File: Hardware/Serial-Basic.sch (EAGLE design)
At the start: 25 parts, among them J1 microB, U1 AP2112-3.3V, U2 CH340G, Y2 12MHz

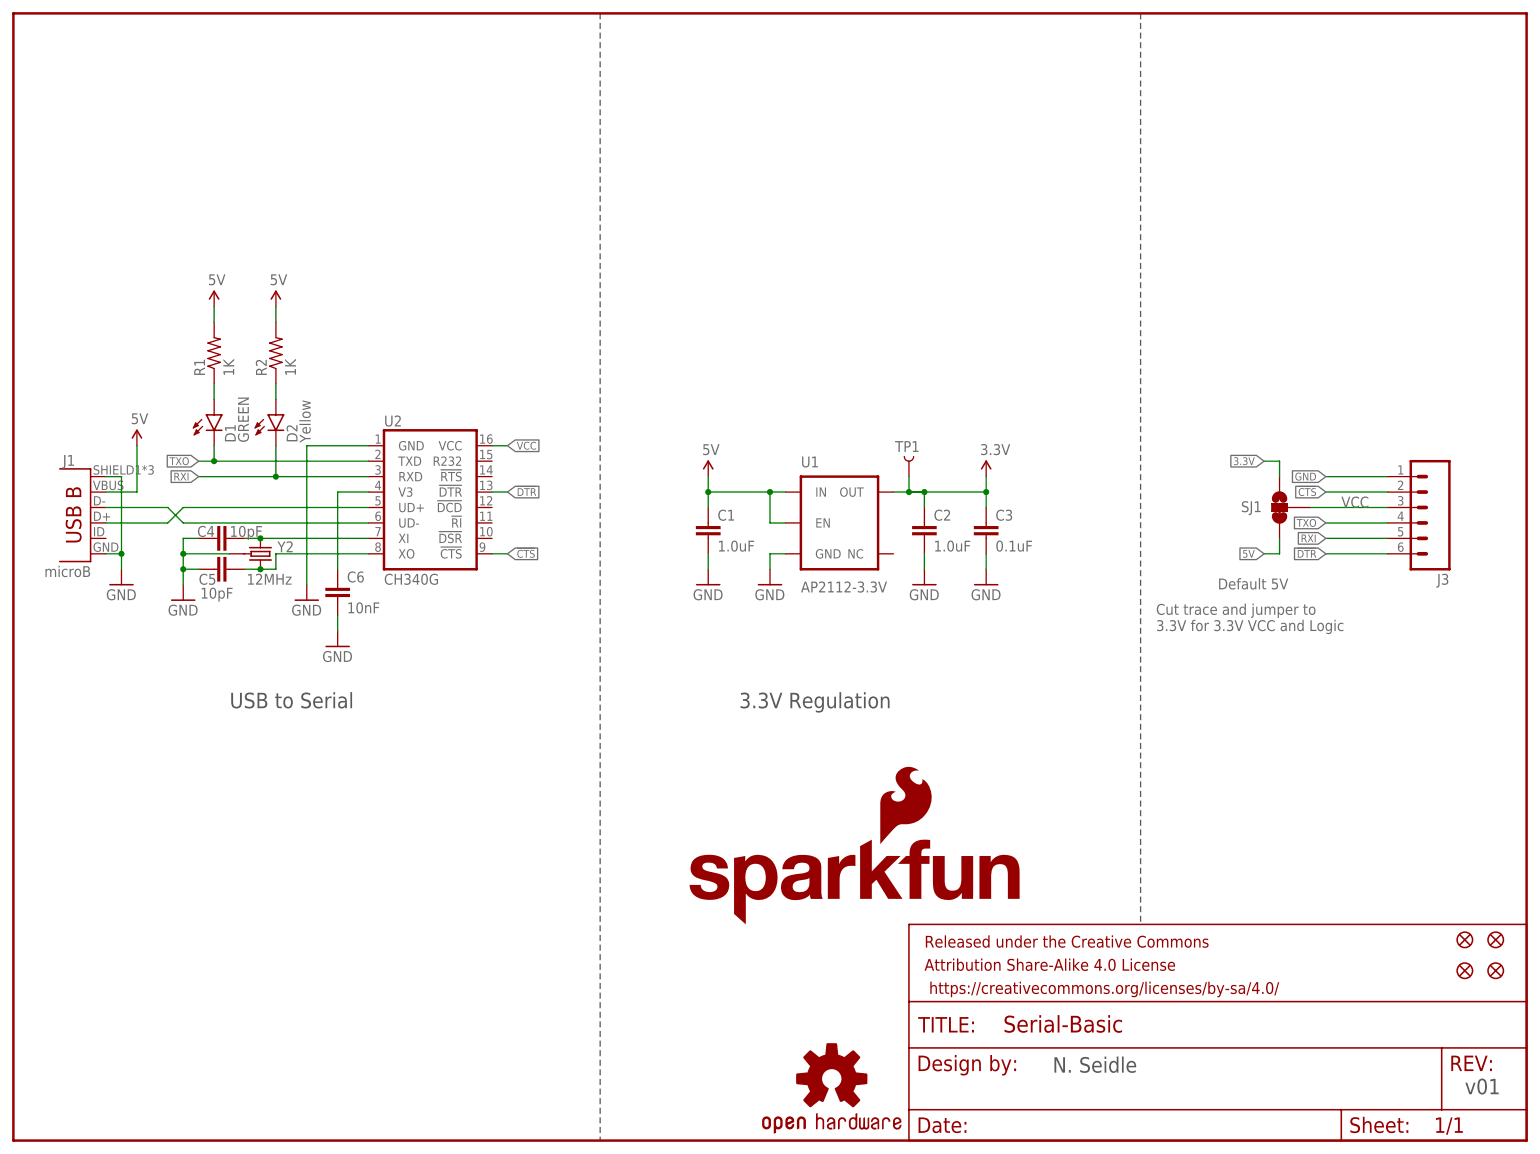
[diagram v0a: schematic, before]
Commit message: Many hardware changes from review.
Moved 0.1uF closer to IC, changed to VCC net. Added via anchors to
microB. Silk bumps. PCB width increase.
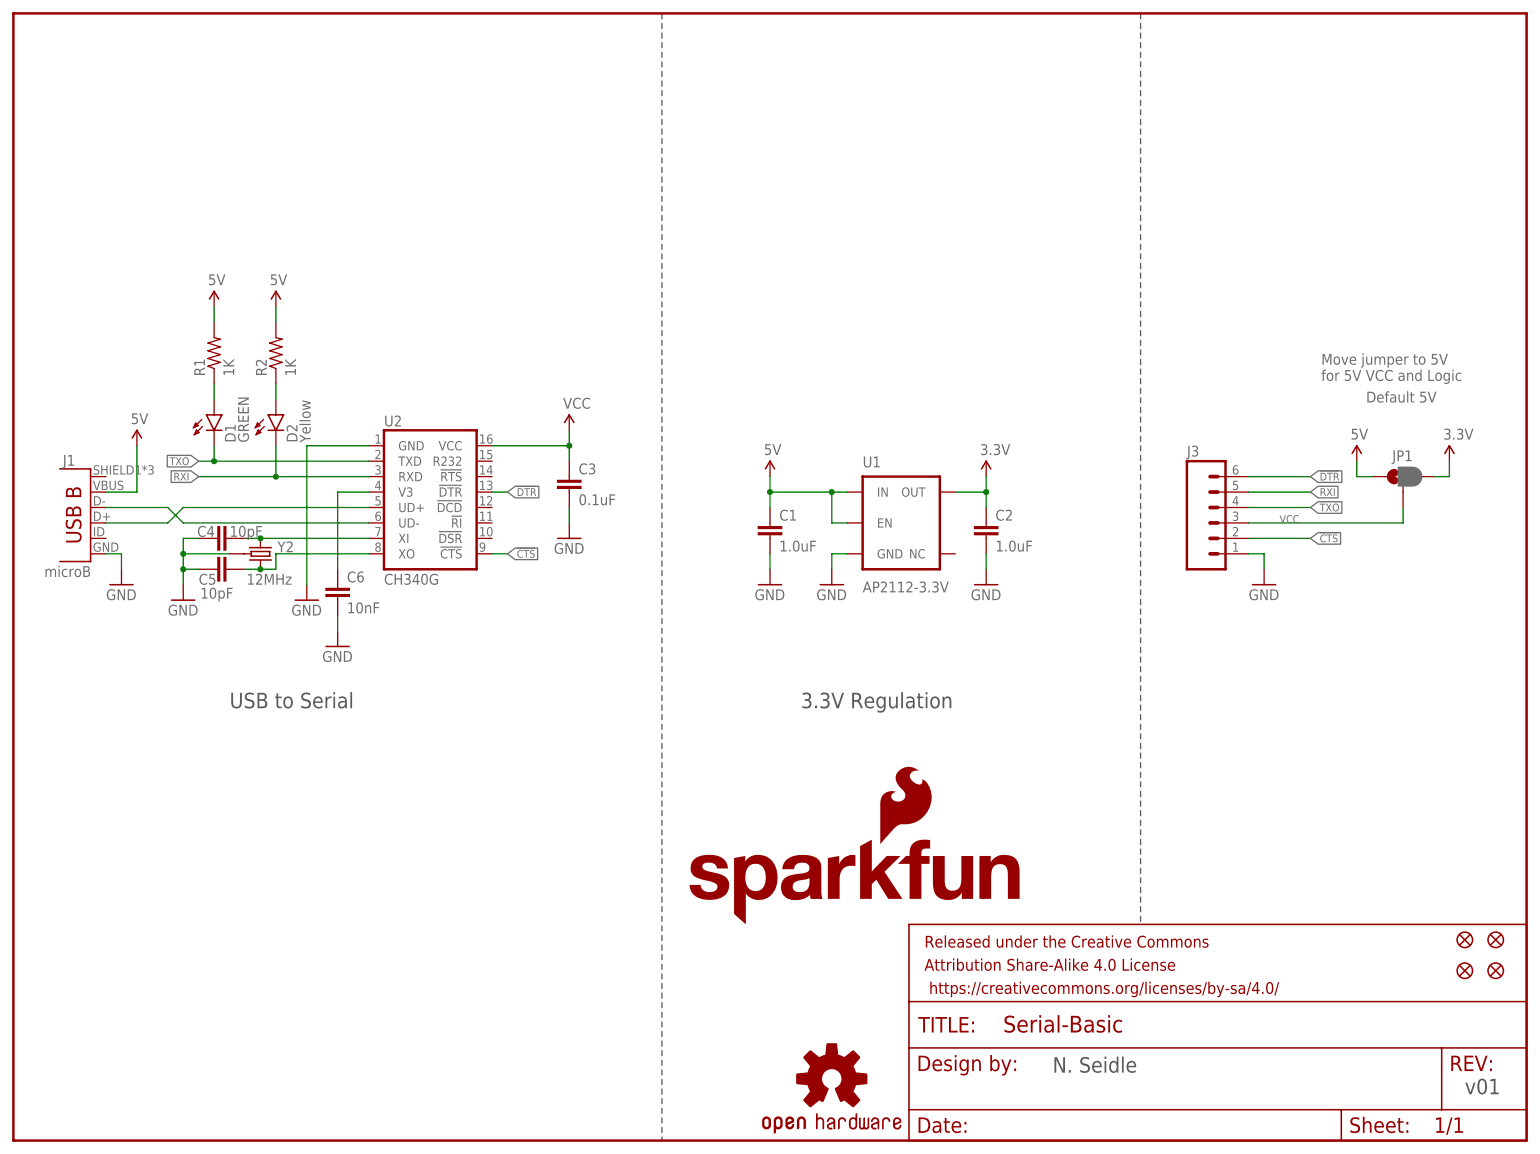
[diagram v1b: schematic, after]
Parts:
- removed SJ1: (no value), SparkFun:SOLDERJUMPER_2WAYS
- removed TP1: 3.3V TP, SparkFun-Passives:TEST-POINT3
- added JP1: JUMPER-PAD-3-2OF3_NC_BY_PASTE, SparkFun-Passives:JUMPER-PAD-3-2OF3_NC_BY_PASTE
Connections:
- net 3.3V: now also JP1.3; no longer C3.1, SJ1.3, TP1.1
- net 5V: now also JP1.1; no longer SJ1.1
- net GND: no longer J1.SHIELD
- net VCC: now also C3.1, JP1.2; no longer SJ1.2
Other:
- note added: "Move jumper to 5V for 5V VCC and Logic"
- note removed: "Cut trace and jumper to 3.3V for 3.3V VCC and Logic"
- moved on the sheet: C1, C2, C3, J3, U1

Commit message: Fixing issues #1, #2, #3, #4
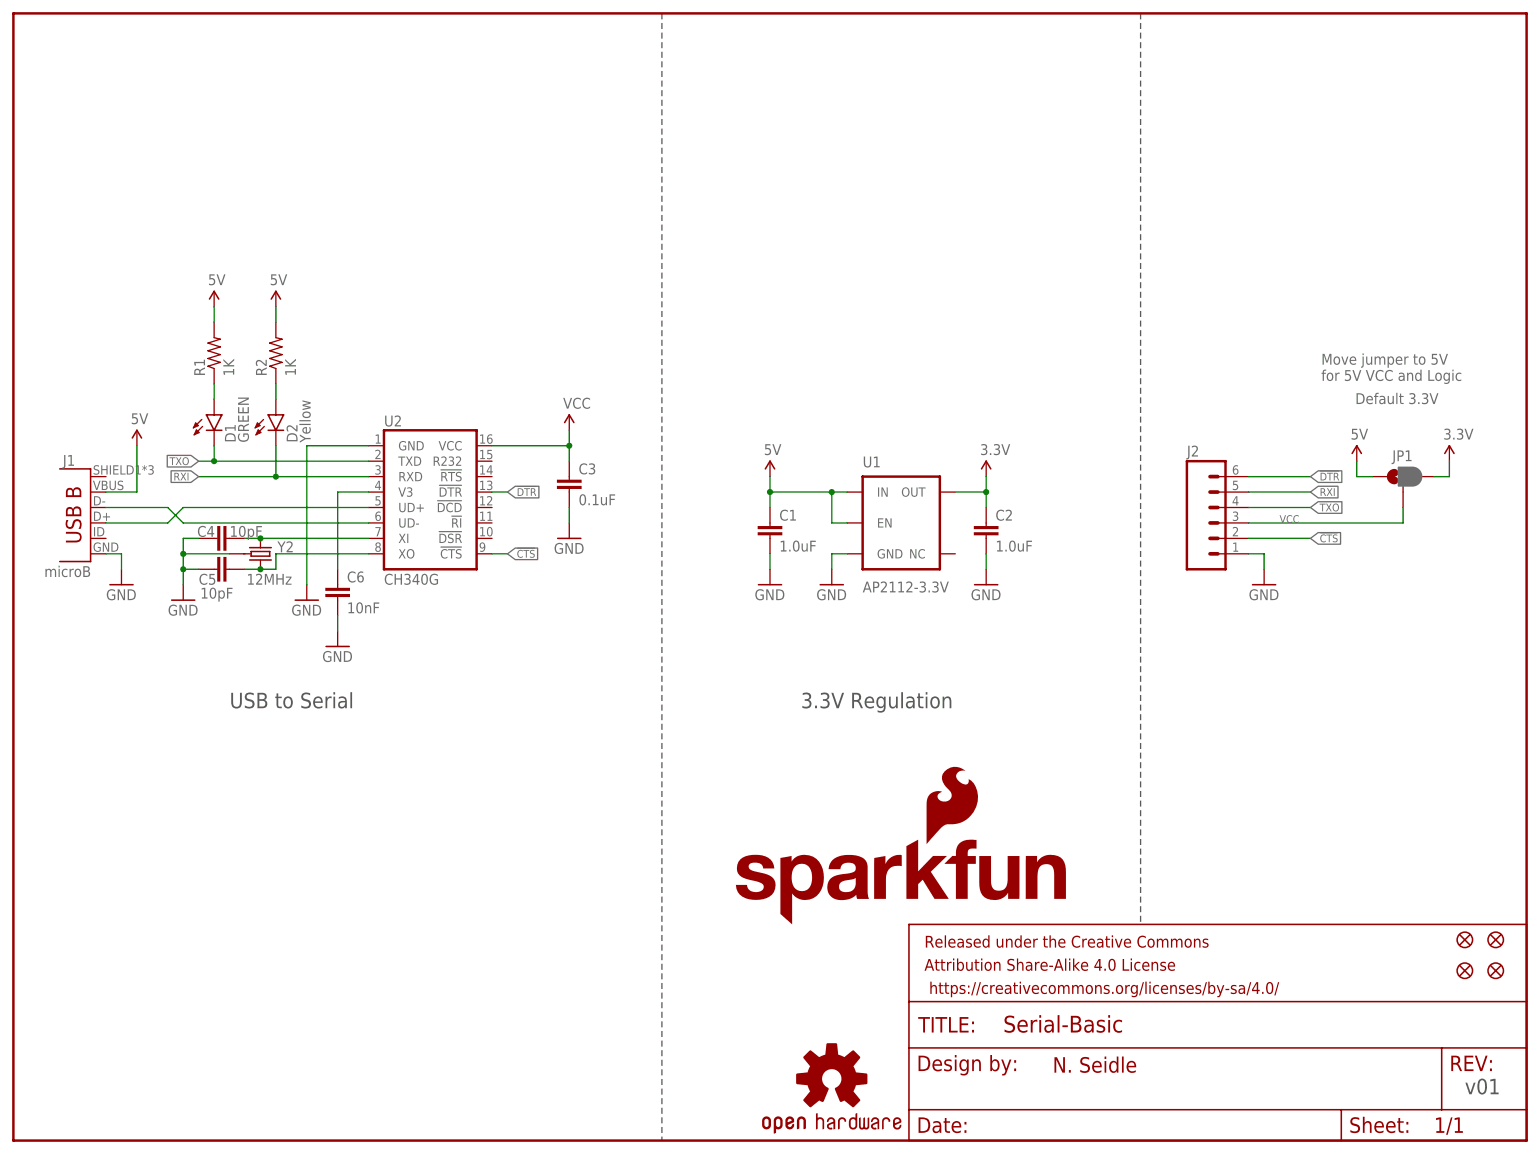
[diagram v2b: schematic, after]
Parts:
- renumbered J3 to J2
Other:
- note added: "Default 3.3V"
- note removed: "Default 5V"
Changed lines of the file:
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@@
 <?xml version="1.0" encoding="utf-8"?>
 <!DOCTYPE eagle SYSTEM "eagle.dtd">
-<eagle version="7.1.0">
+<eagle version="7.2.0">
 <drawing>
 <settings>
@@
 <part name="R2" library="SparkFun-Resistors" deviceset="1KOHM-1/10W-1%(0603)" device="" value="1K"/>
 <part name="C3" library="SparkFun-Capacitors" deviceset="0.1UF-25V(+80/-20%)(0603)" device="" value="0.1uF"/>
-<part name="J3" library="SparkFun-Connectors" deviceset="M06" device="SMD-FEMALE-V2"/>
+<part name="J2" library="SparkFun-Connectors" deviceset="M06" device="SMD-FEMALE-V2"/>
 <part name="SUPPLY2" library="SparkFun-Aesthetics" deviceset="VCC" device=""/>
 <part name="U$2" library="SparkFun" deviceset="5V" device=""/>
@@
 <sheet>
 <plain>
-<text x="222.504" y="121.412" size="1.778" layer="95">Default 5V</text>
+<text x="220.726" y="121.158" size="1.778" layer="95">Default 3.3V</text>
 <text x="238.76" y="7.62" size="2.54" layer="97">v01</text>
 <text x="35.56" y="71.12" size="2.54" layer="97">USB to Serial</text>
@@
 <wire x1="106.68" y1="185.42" x2="106.68" y2="0" width="0.2032" layer="97" style="longdash"/>
 <wire x1="185.42" y1="185.42" x2="185.42" y2="35.56" width="0.2032" layer="97" style="longdash"/>
-<text x="170.942" y="11.176" size="2.54" layer="97">N. Seidle</text>
+<text x="170.942" y="11.176" size="2.54" layer="94">N. Seidle</text>
 <text x="215.138" y="124.968" size="1.778" layer="95">Move jumper to 5V
 for 5V VCC and Logic</text>
@@
 <instance part="GND8" gate="1" x="53.34" y="81.28"/>
 <instance part="SUPPLY1" gate="G$1" x="160.02" y="109.22"/>
-<instance part="LOGO3" gate="G$1" x="109.22" y="35.56"/>
-<instance part="LOGO2" gate="G$1" x="142.24" y="48.26"/>
+<instance part="LOGO3" gate="G$1" x="116.84" y="35.56"/>
+<instance part="LOGO2" gate="G$1" x="149.86" y="48.26"/>
 <instance part="D1" gate="G$1" x="33.02" y="119.38"/>
 <instance part="D2" gate="G$1" x="43.18" y="119.38"/>
@@
 <instance part="R2" gate="G$1" x="43.18" y="129.54" rot="R90"/>
 <instance part="C3" gate="G$1" x="91.44" y="106.68"/>
-<instance part="J3" gate="G$1" x="198.12" y="101.6"/>
+<instance part="J2" gate="G$1" x="198.12" y="101.6"/>
 <instance part="SUPPLY2" gate="G$1" x="91.44" y="116.84"/>
 <instance part="U$2" gate="G$1" x="220.98" y="111.76"/>
@@
 <segment>
 <wire x1="203.2" y1="96.52" x2="205.74" y2="96.52" width="0.1524" layer="91"/>
-<pinref part="J3" gate="G$1" pin="1"/>
+<pinref part="J2" gate="G$1" pin="1"/>
 <pinref part="GND1" gate="1" pin="GND"/>
 <wire x1="205.74" y1="93.98" x2="205.74" y2="96.52" width="0.1524" layer="91"/>
@@
 <wire x1="203.2" y1="99.06" x2="213.36" y2="99.06" width="0.1524" layer="91"/>
 <label x="213.36" y="99.06" size="1.27" layer="95" xref="yes"/>
-<pinref part="J3" gate="G$1" pin="2"/>
+<pinref part="J2" gate="G$1" pin="2"/>
 </segment>
 <segment>
@@
 <wire x1="203.2" y1="109.22" x2="213.36" y2="109.22" width="0.1524" layer="91"/>
 <label x="213.36" y="109.22" size="1.27" layer="95" xref="yes"/>
-<pinref part="J3" gate="G$1" pin="6"/>
+<pinref part="J2" gate="G$1" pin="6"/>
 </segment>
 <segment>
@@
 <wire x1="203.2" y1="104.14" x2="213.36" y2="104.14" width="0.1524" layer="91"/>
 <label x="213.36" y="104.14" size="1.27" layer="95" xref="yes"/>
-<pinref part="J3" gate="G$1" pin="4"/>
+<pinref part="J2" gate="G$1" pin="4"/>
 </segment>
 <segment>
@@
 <wire x1="203.2" y1="106.68" x2="213.36" y2="106.68" width="0.1524" layer="91"/>
 <label x="213.36" y="106.68" size="1.27" layer="95" xref="yes"/>
-<pinref part="J3" gate="G$1" pin="5"/>
+<pinref part="J2" gate="G$1" pin="5"/>
 </segment>
 <segment>
@@
 <segment>
 <label x="208.28" y="101.6" size="1.27" layer="95"/>
-<pinref part="J3" gate="G$1" pin="3"/>
+<pinref part="J2" gate="G$1" pin="3"/>
 <wire x1="203.2" y1="101.6" x2="228.6" y2="101.6" width="0.1524" layer="91"/>
 <wire x1="228.6" y1="101.6" x2="228.6" y2="104.14" width="0.1524" layer="91"/>

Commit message: Changing resistor on Greeg LED to 330
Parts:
- removed R1: 1K, SparkFun-Resistors:1KOHM-1/10W-1%(0603)
- added R3: 330, SparkFun-Resistors:330OHM1/10W1%(0603)
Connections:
- net 5V: no longer R1.2, R2.2
- net N$1: now also R3.1; no longer R1.1
- net VCC: now also R2.2, R3.2
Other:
- note added: "v10"
- note removed: "v01"
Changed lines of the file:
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@@
 <part name="FRAME1" library="SparkFun-Aesthetics" deviceset="FRAME-LETTER" device=""/>
 <part name="GND7" library="SparkFun" deviceset="GND" device=""/>
-<part name="U$1" library="SparkFun" deviceset="5V" device=""/>
-<part name="U$4" library="SparkFun" deviceset="5V" device=""/>
 <part name="JP3" library="SparkFun" deviceset="FIDUCIAL" device="1X2"/>
 <part name="JP4" library="SparkFun" deviceset="FIDUCIAL" device="1X2"/>
@@
 <part name="D1" library="SparkFun-LED" deviceset="LED-GREEN" device="0603" value="GREEN"/>
 <part name="D2" library="SparkFun-LED" deviceset="LED-YELLOW" device="0603" value="Yellow"/>
-<part name="R1" library="SparkFun-Resistors" deviceset="1KOHM-1/10W-1%(0603)" device="" value="1K"/>
 <part name="R2" library="SparkFun-Resistors" deviceset="1KOHM-1/10W-1%(0603)" device="" value="1K"/>
 <part name="C3" library="SparkFun-Capacitors" deviceset="0.1UF-25V(+80/-20%)(0603)" device="" value="0.1uF"/>
@@
 <part name="GND1" library="SparkFun" deviceset="GND" device=""/>
 <part name="JP1" library="SparkFun-Passives" deviceset="JUMPER-PAD-3-2OF3_NC_BY_PASTE" device="" value=""/>
+<part name="SUPPLY4" library="SparkFun-Aesthetics" deviceset="VCC" device=""/>
+<part name="SUPPLY5" library="SparkFun-Aesthetics" deviceset="VCC" device=""/>
+<part name="R3" library="SparkFun-Resistors" deviceset="330OHM1/10W1%(0603)" device="" value="330"/>
 </parts>
 <sheets>
@@
 <plain>
 <text x="220.726" y="121.158" size="1.778" layer="95">Default 3.3V</text>
-<text x="238.76" y="7.62" size="2.54" layer="97">v01</text>
+<text x="238.76" y="7.62" size="2.54" layer="97">v10</text>
 <text x="35.56" y="71.12" size="2.54" layer="97">USB to Serial</text>
 <text x="129.54" y="71.12" size="2.54" layer="97">3.3V Regulation</text>
@@
 <instance part="FRAME1" gate="V" x="147.32" y="0"/>
 <instance part="GND7" gate="1" x="91.44" y="99.06"/>
-<instance part="U$1" gate="G$1" x="33.02" y="137.16"/>
-<instance part="U$4" gate="G$1" x="43.18" y="137.16"/>
 <instance part="JP3" gate="G$1" x="238.76" y="27.94"/>
 <instance part="JP4" gate="G$1" x="243.84" y="27.94"/>
@@
 <instance part="D1" gate="G$1" x="33.02" y="119.38"/>
 <instance part="D2" gate="G$1" x="43.18" y="119.38"/>
-<instance part="R1" gate="G$1" x="33.02" y="129.54" rot="R90"/>
 <instance part="R2" gate="G$1" x="43.18" y="129.54" rot="R90"/>
 <instance part="C3" gate="G$1" x="91.44" y="106.68"/>
@@
 <attribute name="VALUE" x="230.505" y="111.76" size="1.778" layer="96" rot="R90"/>
 </instance>
+<instance part="SUPPLY4" gate="G$1" x="43.18" y="137.16"/>
+<instance part="SUPPLY5" gate="G$1" x="33.02" y="137.16"/>
+<instance part="R3" gate="G$1" x="33.02" y="129.54" rot="R90"/>
 </instances>
 <busses>
@@
 <wire x1="33.02" y1="124.46" x2="33.02" y2="121.92" width="0.1524" layer="91"/>
 <pinref part="D1" gate="G$1" pin="A"/>
-<pinref part="R1" gate="G$1" pin="1"/>
+<pinref part="R3" gate="G$1" pin="1"/>
 </segment>
 </net>
@@
 <wire x1="91.44" y1="116.84" x2="91.44" y2="114.3" width="0.1524" layer="91"/>
 </segment>
+<segment>
+<wire x1="43.18" y1="137.16" x2="43.18" y2="134.62" width="0.1524" layer="91"/>
+<pinref part="R2" gate="G$1" pin="2"/>
+<pinref part="SUPPLY4" gate="G$1" pin="VCC"/>
+</segment>
+<segment>
+<wire x1="33.02" y1="137.16" x2="33.02" y2="134.62" width="0.1524" layer="91"/>
+<pinref part="SUPPLY5" gate="G$1" pin="VCC"/>
+<pinref part="R3" gate="G$1" pin="2"/>
+</segment>
 </net>
 <net name="5V" class="0">
 <segment>
-<wire x1="33.02" y1="137.16" x2="33.02" y2="134.62" width="0.1524" layer="91"/>
-<pinref part="U$1" gate="G$1" pin="5V"/>
-<pinref part="R1" gate="G$1" pin="2"/>
-</segment>
-<segment>
-<wire x1="43.18" y1="137.16" x2="43.18" y2="134.62" width="0.1524" layer="91"/>
-<pinref part="U$4" gate="G$1" pin="5V"/>
-<pinref part="R2" gate="G$1" pin="2"/>
-</segment>
-<segment>
 <wire x1="223.52" y1="109.22" x2="220.98" y2="109.22" width="0.1524" layer="91"/>
